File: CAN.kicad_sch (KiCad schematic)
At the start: 18 parts, among them J21 CAN_IN, J22 CAN_OUT, J26 CAN_TP, U17 ADM3055E, U18 CDSOT23-T24CAN

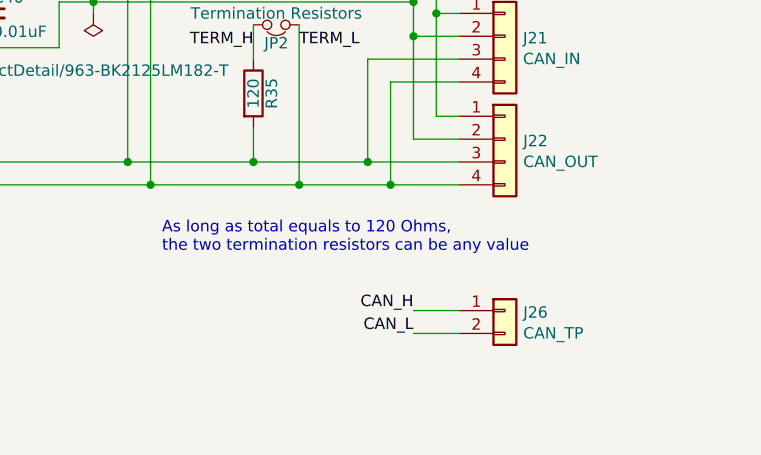
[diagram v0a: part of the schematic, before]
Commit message: Added extra CAN ports for debugging on to schematic.
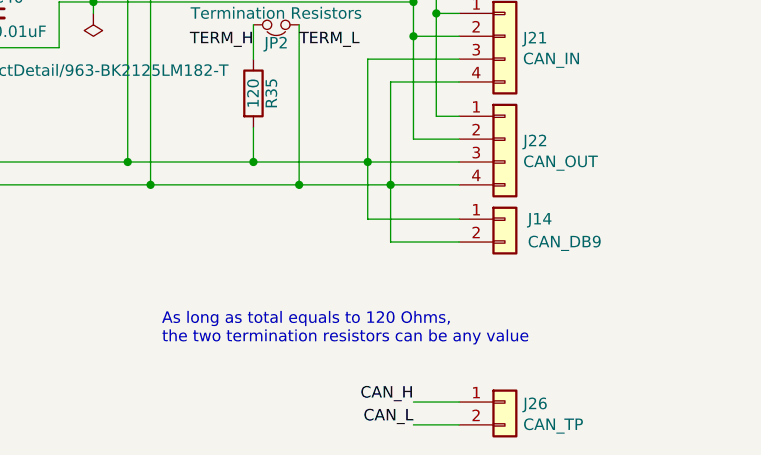
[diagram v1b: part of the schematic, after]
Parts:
- added J14: CAN_DB9, Connector_Molex:Molex_Micro-Fit_3.0_43650-0215_1x02_P3.00mm_Vertical, symbol Connector_Generic:Conn_01x02
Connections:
- net CAN_H: now also J14.1 (Pin_1)
- net CAN_L: now also J14.2 (Pin_2)
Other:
- moved on the sheet: J26
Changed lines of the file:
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@@
 	(wire
 		(pts
+			(xy 218.44 106.68) (xy 226.06 106.68)
+		)
+		(stroke
+			(width 0)
+			(type default)
+		)
+	)
+	(wire
+		(pts
 			(xy 133.35 77.47) (xy 146.05 77.47)
 		)
@@
 	(wire
 		(pts
+			(xy 215.9 104.14) (xy 226.06 104.14)
+		)
+		(stroke
+			(width 0)
+			(type default)
+		)
+	)
+	(wire
+		(pts
 			(xy 153.67 85.09) (xy 156.21 85.09)
 		)
@@
 	(wire
 		(pts
+			(xy 218.44 100.33) (xy 218.44 106.68)
+		)
+		(stroke
+			(width 0)
+			(type default)
+		)
+	)
+	(wire
+		(pts
 			(xy 226.06 81.28) (xy 223.52 81.28)
 		)
@@
 	(wire
 		(pts
-			(xy 226.06 116.84) (xy 220.98 116.84)
+			(xy 226.06 127) (xy 220.98 127)
 		)
 		(stroke
@@
 	(wire
 		(pts
+			(xy 215.9 97.79) (xy 215.9 104.14)
+		)
+		(stroke
+			(width 0)
+			(type default)
+		)
+	)
+	(wire
+		(pts
 			(xy 173.99 77.47) (xy 185.42 77.47)
 		)
@@
 	(wire
 		(pts
-			(xy 226.06 114.3) (xy 220.98 114.3)
+			(xy 226.06 124.46) (xy 220.98 124.46)
 		)
 		(stroke
@@
 	(text "As long as total equals to 120 Ohms,\nthe two termination resistors can be any value"
 		(exclude_from_sim no)
-		(at 193.04 107.95 0)
+		(at 193.04 118.11 0)
 		(effects
 			(font
@@
 	)
 	(label "CAN_L"
-		(at 220.98 116.84 180)
+		(at 220.98 127 180)
 		(fields_autoplaced yes)
 		(effects
@@
 	)
 	(label "CAN_H"
-		(at 220.98 114.3 180)
+		(at 220.98 124.46 180)
 		(fields_autoplaced yes)
 		(effects
@@
 	(symbol
 		(lib_id "Connector_Generic:Conn_01x02")
-		(at 231.14 114.3 0)
+		(at 231.14 124.46 0)
 		(unit 1)
 		(exclude_from_sim no)
@@
 		(dnp no)
 		(property "Reference" "J26"
-			(at 233.172 114.5032 0)
+			(at 233.172 124.6632 0)
 			(effects
 				(font
@@
 		)
 		(property "Value" "CAN_TP"
-			(at 233.172 116.8146 0)
+			(at 233.172 126.9746 0)
 			(effects
 				(font
@@
 		)
 		(property "Footprint" "Connector_PinHeader_2.54mm:PinHeader_1x02_P2.54mm_Vertical"
-			(at 231.14 114.3 0)
+			(at 231.14 124.46 0)
 			(effects
 				(font
@@
 		)
 		(property "Datasheet" "~"
-			(at 231.14 114.3 0)
+			(at 231.14 124.46 0)
 			(effects
 				(font
@@
 		)
 		(property "Description" "Generic connector, single row, 01x02, script generated (kicad-library-utils/schlib/autogen/connector/)"
-			(at 231.14 114.3 0)
+			(at 231.14 124.46 0)
 			(effects
 				(font
@@
 		)
 		(property "Id" ""
-			(at 231.14 114.3 0)
+			(at 231.14 124.46 0)
 			(effects
 				(font
@@
 		)
 		(property "Vds" ""
-			(at 231.14 114.3 0)
+			(at 231.14 124.46 0)
 			(effects
 				(font
@@
 					(unit 1)
 				)
+			)
+		)
+	)
+	(symbol
+		(lib_id "Connector_Generic:Conn_01x02")
+		(at 231.14 104.14 0)
+		(unit 1)
+		(exclude_from_sim no)
+		(in_bom yes)
+		(on_board yes)
+		(dnp no)
+		(fields_autoplaced yes)
+		(property "Reference" "J14"
+			(at 233.68 104.1399 0)
+			(effects
+				(font
+					(size 1.27 1.27)
+				)
+				(justify left)
+			)
+		)
+		(property "Value" "CAN_DB9"
+			(at 233.68 106.6799 0)
+			(effects
+				(font
+					(size 1.27 1.27)
+				)
+				(justify left)
+			)
+		)
+		(property "Footprint" "Connector_Molex:Molex_Micro-Fit_3.0_43650-0215_1x02_P3.00mm_Vertical"
+			(at 231.14 104.14 0)
+			(effects
+				(font
+					(size 1.27 1.27)
+				)
+				(hide yes)
+			)
+		)
+		(property "Datasheet" "~"
+			(at 231.14 104.14 0)
+			(effects
+				(font
+					(size 1.27 1.27)
+				)
+				(hide yes)
+			)
+		)
+		(property "Description" "Generic connector, single row, 01x02, script generated (kicad-library-utils/schlib/autogen/connector/)"
+			(at 231.14 104.14 0)
+			(effects
+				(font
+					(size 1.27 1.27)
+				)
+				(hide yes)
+			)
+		)
+		(pin "2"
+		)
+		(pin "1"
+		)
+		(instances
+			(project ""
+				(path "/66218487-e316-4467-9eba-79d4626ab24e/00000000-0000-0000-0000-00005f547b94"
+					(reference "J14")
+					(unit 1)
+				)

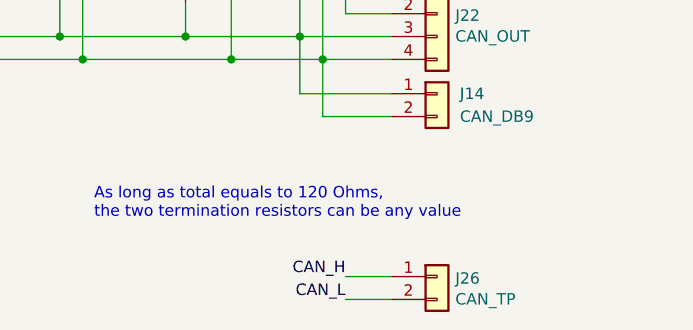
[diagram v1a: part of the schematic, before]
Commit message: More routing, updated board constraints.
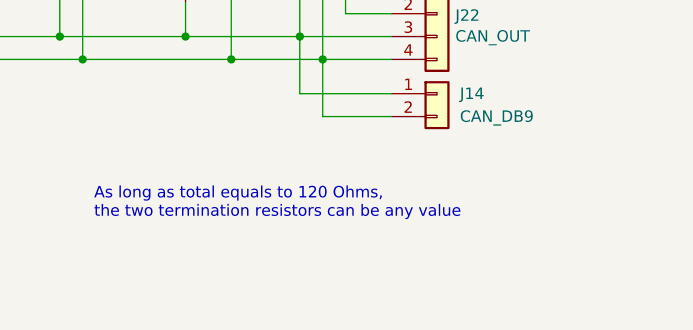
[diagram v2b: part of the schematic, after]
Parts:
- removed J26: CAN_TP, Connector_PinHeader_2.54mm:PinHeader_1x02_P2.54mm_Vertical, symbol Connector_Generic:Conn_01x02
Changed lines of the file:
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@@
-	(wire
-		(pts
-			(xy 226.06 127) (xy 220.98 127)
-		)
-		(stroke
-			(width 0)
-			(type default)
-		)
-	)
 	(wire
 		(pts
@@
 		(pts
 			(xy 128.27 100.33) (xy 191.77 100.33)
-		)
-		(stroke
-			(width 0)
-			(type default)
-		)
-	)
-	(wire
-		(pts
-			(xy 226.06 124.46) (xy 220.98 124.46)
 		)
 		(stroke
@@
 		)
 	)
-	(label "CAN_L"
-		(at 220.98 127 180)
-		(fields_autoplaced yes)
-		(effects
-			(font
-				(size 1.27 1.27)
-			)
-			(justify right bottom)
-		)
-	)
 	(label "RSlope"
 		(at 128.27 105.41 0)
@@
 			)
 			(justify left bottom)
-		)
-	)
-	(label "CAN_H"
-		(at 220.98 124.46 180)
-		(fields_autoplaced yes)
-		(effects
-			(font
-				(size 1.27 1.27)
-			)
-			(justify right bottom)
 		)
 	)
@@
 					(unit 1)
 				)
-			)
-		)
-	)
-	(symbol
-		(lib_id "Connector_Generic:Conn_01x02")
-		(at 231.14 124.46 0)
-		(unit 1)
-		(exclude_from_sim no)
-		(in_bom yes)
-		(on_board yes)
-		(dnp no)
-		(property "Reference" "J26"
-			(at 233.172 124.6632 0)
-			(effects
-				(font
-					(size 1.27 1.27)
-				)
-				(justify left)
-			)
-		)
-		(property "Value" "CAN_TP"
-			(at 233.172 126.9746 0)
-			(effects
-				(font
-					(size 1.27 1.27)
-				)
-				(justify left)
-			)
-		)
-		(property "Footprint" "Connector_PinHeader_2.54mm:PinHeader_1x02_P2.54mm_Vertical"
-			(at 231.14 124.46 0)
-			(effects
-				(font
-					(size 1.27 1.27)
-				)
-				(hide yes)
-			)
-		)
-		(property "Datasheet" "~"
-			(at 231.14 124.46 0)
-			(effects
-				(font
-					(size 1.27 1.27)
-				)
-				(hide yes)
-			)
-		)
-		(property "Description" "Generic connector, single row, 01x02, script generated (kicad-library-utils/schlib/autogen/connector/)"
-			(at 231.14 124.46 0)
-			(effects
-				(font
-					(size 1.27 1.27)
-				)
-				(hide yes)
-			)
-		)
-		(property "Id" ""
-			(at 231.14 124.46 0)
-			(effects
-				(font
-					(size 1.27 1.27)
-				)
-				(hide yes)
-			)
-		)
-		(property "Vds" ""
-			(at 231.14 124.46 0)
-			(effects
-				(font
-					(size 1.27 1.27)
-				)
-				(hide yes)
-			)
-		)
-		(pin "1"
-		)
-		(pin "2"
-		)
-		(instances
-			(project "Controls-Leader"
-				(path "/66218487-e316-4467-9eba-79d4626ab24e/00000000-0000-0000-0000-00005f547b94"
-					(reference "J26")
-					(unit 1)
-				)

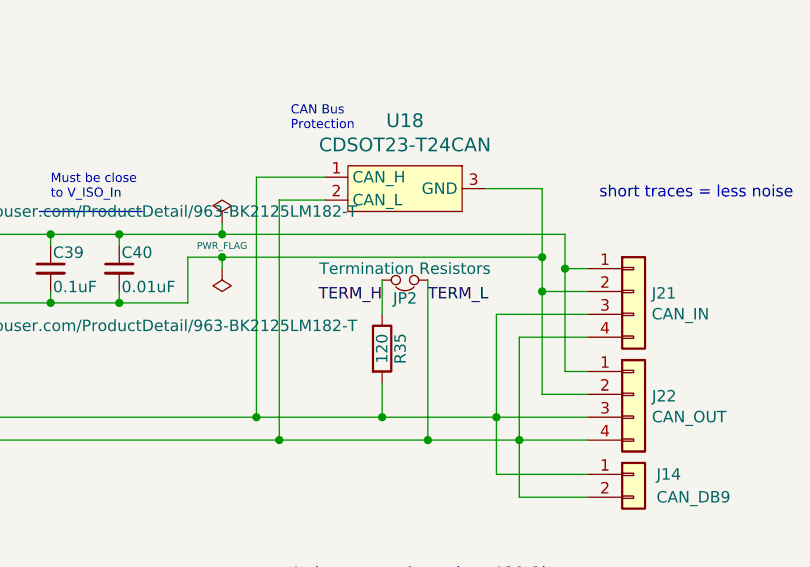
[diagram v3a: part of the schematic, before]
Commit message: Updated some symbols to use common libraries (and get rid of warnings.
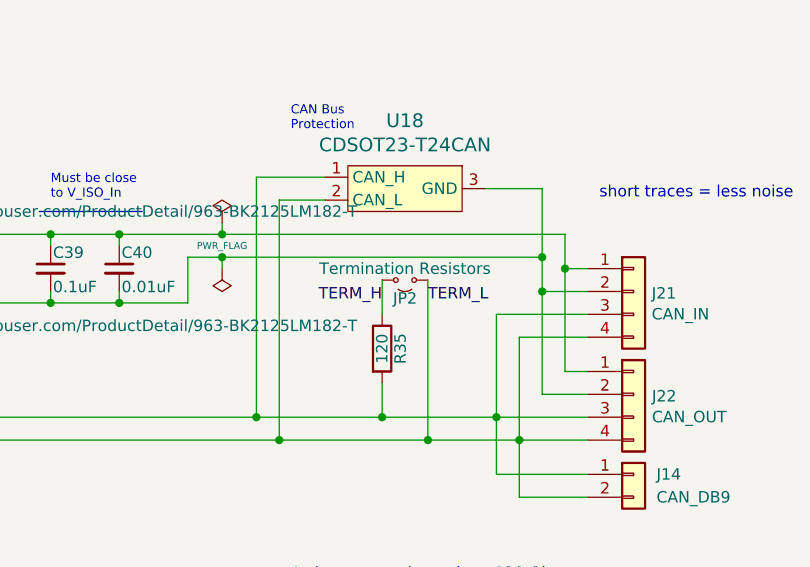
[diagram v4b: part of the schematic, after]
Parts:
- JP2: symbol Device:Jumper_NC_Small -> Jumper:Jumper_2_Small_Open
- L7, L8: symbol Device:Ferrite_Bead_Small -> Device:FerriteBead_Small
- U17: symbol Dashboard-rescue:ADM3055E-utsvt-chips -> utsvt-chips:ADM3055E
- U18: symbol Dashboard-rescue:CDSOT23-T24CAN-utsvt-chips -> utsvt-chips:CDSOT23-T24CAN
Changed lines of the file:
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@@
 	)
 	(symbol
-		(lib_id "Device:Jumper_NC_Small")
+		(lib_id "Jumper:Jumper_2_Small_Open")
 		(at 205.74 82.55 180)
 		(unit 1)
@@
 	)
 	(symbol
-		(lib_id "Device:Ferrite_Bead_Small")
+		(lib_id "Device:FerriteBead_Small")
 		(at 151.13 77.47 270)
 		(unit 1)
@@
 	)
 	(symbol
-		(lib_id "Device:Ferrite_Bead_Small")
+		(lib_id "Device:FerriteBead_Small")
 		(at 151.13 85.09 270)
 		(unit 1)
@@
 	)
 	(symbol
-		(lib_id "Dashboard-rescue:ADM3055E-utsvt-chips")
+		(lib_id "utsvt-chips:ADM3055E")
 		(at 110.49 91.44 0)
 		(unit 1)
@@
 	)
 	(symbol
-		(lib_id "Dashboard-rescue:CDSOT23-T24CAN-utsvt-chips")
+		(lib_id "utsvt-chips:CDSOT23-T24CAN")
 		(at 205.74 72.39 0)
 		(unit 1)

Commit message: Updated comments.
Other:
- note added: "Added J14 CAN_DB9"
- note removed: "No change required"
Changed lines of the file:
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@@
 		)
 	)
-	(text "No change required\n"
-		(exclude_from_sim no)
-		(at 15.24 21.59 0)
+	(text "Added J14 CAN_DB9"
+		(exclude_from_sim no)
+		(at 178.054 180.594 0)
 		(effects
 			(font
 				(face "KiCad Font")
-				(size 5 5)
+				(size 1.524 1.524)
 				(thickness 1)
 				(bold yes)
@@
 				)
 				(justify left)
+				(hide yes)
 			)
 		)
@@
 				)
 				(justify left)
-			)
-		)
+				(hide yes)
+			)
+		)

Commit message: Replaced unavailable parts
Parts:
- L7, L8: value https://www.mouser.com/ProductDetail/963-BK2125LM182-T -> 1.8k; Mouser Part Number BKH1005LM182-T -> 710-742792090; P/N (none) -> 742792090
- U18: footprint Package_TO_SOT_SMD:SOT-23W -> Package_TO_SOT_SMD:SOT-23-3
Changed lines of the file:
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@@
+			)
+		)
+		(property "Digikey" ""
+			(at 203.2 90.17 0)
+			(effects
+				(font
+					(size 1.27 1.27)
+				)
+				(hide yes)
 			)
 		)
@@
 			)
 		)
+		(property "Digikey" ""
+			(at 205.74 82.55 0)
+			(effects
+				(font
+					(size 1.27 1.27)
+				)
+				(hide yes)
+			)
+		)
 		(pin "1"
 		)
@@
 			)
 		)
+		(property "Digikey" ""
+			(at 54.61 85.09 0)
+			(effects
+				(font
+					(size 1.27 1.27)
+				)
+				(hide yes)
+			)
+		)
 		(pin "1"
 		)
@@
 			)
 		)
+		(property "Digikey" ""
+			(at 63.5 85.09 0)
+			(effects
+				(font
+					(size 1.27 1.27)
+				)
+				(hide yes)
+			)
+		)
 		(pin "1"
 		)
@@
 			)
 		)
+		(property "Digikey" ""
+			(at 74.93 85.09 0)
+			(effects
+				(font
+					(size 1.27 1.27)
+				)
+				(hide yes)
+			)
+		)
 		(pin "1"
 		)
@@
 			)
 		)
+		(property "Digikey" ""
+			(at 83.82 85.09 0)
+			(effects
+				(font
+					(size 1.27 1.27)
+				)
+				(hide yes)
+			)
+		)
 		(pin "1"
 		)
@@
 			)
 		)
+		(property "Digikey" ""
+			(at 156.21 81.28 0)
+			(effects
+				(font
+					(size 1.27 1.27)
+				)
+				(hide yes)
+			)
+		)
 		(pin "1"
 		)
@@
 			)
 		)
+		(property "Digikey" ""
+			(at 146.05 81.28 0)
+			(effects
+				(font
+					(size 1.27 1.27)
+				)
+				(hide yes)
+			)
+		)
 		(pin "1"
 		)
@@
 			)
 		)
-		(property "Value" "https://www.mouser.com/ProductDetail/963-BK2125LM182-T"
+		(property "Value" "1.8k"
 			(at 147.32 74.93 90)
 			(effects
@@
 			)
 		)
-		(property "Datasheet" "https://www.mouser.com/ProductDetail/TAIYO-YUDEN/BK2125LM182-T?qs=I6KAKw0tg2wTd%252Bj343lu1Q%3D%3D&srsltid=AfmBOorkhsm8Uk29brVkfBS5oJy8t8TPSw1gIhtEERu0OY8r33ydtYfJ"
+		(property "Datasheet" "https://www.mouser.com/ProductDetail/Wurth-Elektronik/742792090?qs=5twSNpOB8IB2sNFtiBxEew%3D%3D"
 			(at 151.13 77.47 0)
 			(effects
@@
 			)
 		)
-		(property "Mouser Part Number" "BKH1005LM182-T "
+		(property "Mouser Part Number" "710-742792090"
 			(at 151.13 77.47 0)
 			(effects
@@
 			)
 		)
+		(property "Digikey" ""
+			(at 151.13 77.47 0)
+			(effects
+				(font
+					(size 1.27 1.27)
+				)
+				(hide yes)
+			)
+		)
+		(property "P/N" " 742792090"
+			(at 151.13 77.47 0)
+			(effects
+				(font
+					(size 1.27 1.27)
+				)
+				(hide yes)
+			)
+		)
 		(pin "1"
 		)
@@
 			)
 		)
-		(property "Value" "https://www.mouser.com/ProductDetail/963-BK2125LM182-T"
+		(property "Value" "1.8k"
 			(at 147.32 87.63 90)
 			(effects
@@
 			)
 		)
-		(property "Datasheet" "https://www.mouser.com/ProductDetail/TAIYO-YUDEN/BK2125LM182-T?qs=I6KAKw0tg2wTd%252Bj343lu1Q%3D%3D&srsltid=AfmBOorkhsm8Uk29brVkfBS5oJy8t8TPSw1gIhtEERu0OY8r33ydtYfJ"
+		(property "Datasheet" "https://www.mouser.com/ProductDetail/Wurth-Elektronik/742792090?qs=5twSNpOB8IB2sNFtiBxEew%3D%3D"
 			(at 151.13 85.09 0)
 			(effects
@@
 			)
 		)
-		(property "Mouser Part Number" "BKH1005LM182-T "
+		(property "Mouser Part Number" "710-742792090"
 			(at 151.13 85.09 0)
 			(effects
@@
 			)
 		)
+		(property "Digikey" ""
+			(at 151.13 85.09 0)
+			(effects
+				(font
+					(size 1.27 1.27)
+				)
+				(hide yes)
+			)
+		)
+		(property "P/N" " 742792090"
+			(at 151.13 85.09 0)
+			(effects
+				(font
+					(size 1.27 1.27)
+				)
+				(hide yes)
+			)
+		)
 		(pin "1"
 		)
@@
 			)
 		)
+		(property "Digikey" ""
+			(at 166.37 81.28 0)
+			(effects
+				(font
+					(size 1.27 1.27)
+				)
+				(hide yes)
+			)
+		)
 		(pin "1"
 		)
@@
 			)
 		)
+		(property "Digikey" ""
+			(at 173.99 81.28 0)
+			(effects
+				(font
+					(size 1.27 1.27)
+				)
+				(hide yes)
+			)
+		)
 		(pin "1"
 		)
@@
 			)
 		)
+		(property "Digikey" ""
+			(at 140.97 105.41 0)
+			(effects
+				(font
+					(size 1.27 1.27)
+				)
+				(hide yes)
+			)
+		)
 		(pin "1"
 		)
@@
 			)
 		)
+		(property "Digikey" ""
+			(at 231.14 83.82 0)
+			(effects
+				(font
+					(size 1.27 1.27)
+				)
+				(hide yes)
+			)
+		)
 		(pin "1"
 		)
@@
 			)
 		)
+		(property "Digikey" ""
+			(at 231.14 95.25 0)
+			(effects
+				(font
+					(size 1.27 1.27)
+				)
+				(hide yes)
+			)
+		)
 		(pin "1"
 		)
@@
 			)
 		)
+		(property "Digikey" ""
+			(at 110.49 91.44 0)
+			(effects
+				(font
+					(size 1.27 1.27)
+				)
+				(hide yes)
+			)
+		)
 		(pin "1"
 		)
@@
 			)
 		)
-		(property "Footprint" "Package_TO_SOT_SMD:SOT-23W"
+		(property "Footprint" "Package_TO_SOT_SMD:SOT-23-3"
 			(at 205.74 72.39 0)
 			(effects
@@
 			)
 		)
-		(property "Datasheet" ""
+		(property "Datasheet" "https://www.mouser.com/ProductDetail/Bourns/CDSOT23-T24CAN?qs=Z7P4xsdcg2LuAOb%2FzQ7xoQ%3D%3D&srsltid=AfmBOoo-PAeiWAfgofEpaXl2YTbs5tzVBFt4xpFaZPxBSWl1qHW5CPZ0"
 			(at 205.74 72.39 0)
 			(effects
@@
 		)
 		(property "Vds" ""
+			(at 205.74 72.39 0)
+			(effects
+				(font
+					(size 1.27 1.27)
+				)
+				(hide yes)
+			)
+		)
+		(property "Digikey" ""
 			(at 205.74 72.39 0)
 			(effects
@@
 			(at 231.14 104.14 0)
 			(effects
+				(font
+					(size 1.27 1.27)
+				)
+				(hide yes)
+			)
+		)
+		(property "Digikey" ""
+			(at 231.14 104.14 0)
+			(effects

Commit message: Filled in part numbers, exported BOM and made Excel file for working with it.
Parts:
- C33, C38: P/N (none) -> TMK212BBJ106MGHT
- C34, C35, C39: P/N (none) -> C0805C104M5R
- C36, C40: Mouser Part Number C0805C103J5RACTU -> (none); P/N (none) -> C0805C103J5RACTU
- C37: P/N (none) -> C0805C224J1RECTU
- J14: P/N (none) -> 436500215
- J21, J22: P/N (none) -> 436500244
- R34: P/N (none) -> CRCW08050000Z0EAC
- R35: Mouser Part Number CRCW0805120RFKEA -> (none); P/N (none) -> CRCW0805120RFKEA
- U18: P/N (none) -> CDSOT23-T24CAN
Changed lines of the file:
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@@
 			)
 		)
-		(property "Mouser Part Number" "CRCW0805120RFKEA"
+		(property "Mouser Part Number" ""
 			(at 203.2 90.17 0)
 			(effects
@@
 		)
 		(property "Digikey" ""
+			(at 203.2 90.17 0)
+			(effects
+				(font
+					(size 1.27 1.27)
+				)
+				(hide yes)
+			)
+		)
+		(property "P/N" "CRCW0805120RFKEA"
 			(at 203.2 90.17 0)
 			(effects
@@
 			)
 		)
-		(property "Datasheet" ""
+		(property "Datasheet" "https://www.molex.com/en-us/products/part-detail/436500215"
 			(at 205.74 82.55 0)
 			(effects
@@
 			)
 		)
+		(property "P/N" "TMK212BBJ106MGHT"
+			(at 54.61 85.09 0)
+			(effects
+				(font
+					(size 1.27 1.27)
+				)
+				(hide yes)
+			)
+		)
 		(pin "1"
 		)
@@
 			)
 		)
+		(property "P/N" "C0805C104M5R"
+			(at 63.5 85.09 0)
+			(effects
+				(font
+					(size 1.27 1.27)
+				)
+				(hide yes)
+			)
+		)
 		(pin "1"
 		)
@@
 			)
 		)
+		(property "P/N" "C0805C104M5R"
+			(at 74.93 85.09 0)
+			(effects
+				(font
+					(size 1.27 1.27)
+				)
+				(hide yes)
+			)
+		)
 		(pin "1"
 		)
@@
 			)
 		)
-		(property "Mouser Part Number" "C0805C103J5RACTU"
+		(property "Mouser Part Number" ""
 			(at 83.82 85.09 0)
 			(effects
@@
 		)
 		(property "Digikey" ""
+			(at 83.82 85.09 0)
+			(effects
+				(font
+					(size 1.27 1.27)
+				)
+				(hide yes)
+			)
+		)
+		(property "P/N" "C0805C103J5RACTU"
 			(at 83.82 85.09 0)
 			(effects
@@
 			)
 		)
+		(property "P/N" "TMK212BBJ106MGHT"
+			(at 156.21 81.28 0)
+			(effects
+				(font
+					(size 1.27 1.27)
+				)
+				(hide yes)
+			)
+		)
 		(pin "1"
 		)
@@
 			)
 		)
+		(property "P/N" "C0805C224J1RECTU"
+			(at 146.05 81.28 0)
+			(effects
+				(font
+					(size 1.27 1.27)
+				)
+				(hide yes)
+			)
+		)
 		(pin "1"
 		)
@@
 			)
 		)
+		(property "P/N" "C0805C104M5R"
+			(at 166.37 81.28 0)
+			(effects
+				(font
+					(size 1.27 1.27)
+				)
+				(hide yes)
+			)
+		)
 		(pin "1"
 		)
@@
 			)
 		)
-		(property "Mouser Part Number" "C0805C103J5RACTU"
+		(property "Mouser Part Number" ""
 			(at 173.99 81.28 0)
 			(effects
@@
 		)
 		(property "Digikey" ""
+			(at 173.99 81.28 0)
+			(effects
+				(font
+					(size 1.27 1.27)
+				)
+				(hide yes)
+			)
+		)
+		(property "P/N" "C0805C103J5RACTU"
 			(at 173.99 81.28 0)
 			(effects
@@
 			)
 		)
+		(property "P/N" "CRCW08050000Z0EAC "
+			(at 140.97 105.41 0)
+			(effects
+				(font
+					(size 1.27 1.27)
+				)
+				(hide yes)
+			)
+		)
 		(pin "1"
 		)
@@
 			)
 		)
+		(property "P/N" "436500244"
+			(at 231.14 83.82 0)
+			(effects
+				(font
+					(size 1.27 1.27)
+				)
+				(hide yes)
+			)
+		)
 		(pin "1"
 		)
@@
 			)
 		)
+		(property "P/N" "436500244"
+			(at 231.14 95.25 0)
+			(effects
+				(font
+					(size 1.27 1.27)
+				)
+				(hide yes)
+			)
+		)
 		(pin "1"
 		)
@@
 		)
 		(property "Digikey" ""
+			(at 205.74 72.39 0)
+			(effects
+				(font
+					(size 1.27 1.27)
+				)
+				(hide yes)
+			)
+		)
+		(property "P/N" "CDSOT23-T24CAN "
 			(at 205.74 72.39 0)
 			(effects
@@
 			)
 		)
-		(property "Datasheet" "~"
+		(property "Datasheet" "https://www.molex.com/en-us/products/part-detail/436500215"
 			(at 231.14 104.14 0)
 			(effects
@@
 			(at 231.14 104.14 0)
 			(effects
+				(font
+					(size 1.27 1.27)
+				)
+				(hide yes)
+			)
+		)
+		(property "P/N" "436500215"
+			(at 231.14 104.14 0)
+			(effects

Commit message: Added version update notes.
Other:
- note added: "- Added J14 CAN_DB9 for debugging - Removed testpoint - Chose new ferrite beads"
- note removed: "Added J14 CAN_DB9"
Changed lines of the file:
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@@
 		)
 	)
-	(text "Added J14 CAN_DB9"
+	(text "- Added J14 CAN_DB9 for debugging\n- Removed testpoint\n- Chose new ferrite beads"
 		(exclude_from_sim no)
 		(at 178.054 180.594 0)
@@
 				(face "KiCad Font")
 				(size 1.524 1.524)
-				(thickness 1)
-				(bold yes)
+				(thickness 0.1905)
 				(color 255 2 13 1)
 			)
